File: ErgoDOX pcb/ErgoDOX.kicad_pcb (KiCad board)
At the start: 2 copper layers, 182.8 x 158.9 mm, 77 parts, among them J1 USB, J2 3.5mm, J3 JMP, J4 JMP, SW0:10 SW0:3, SW0:11 SW0:2, SW0:12 SW0:1, SW0:7 SW0:6, SW0:8 SW0:5, SW0:9 SW0:4, SW1:10 SW1:3, SW1:11 SW1:2, SW1:12 SW1:1, SW1:13 SW1:0, SW1:9 SW1:4, SW2:10 SW2:3, SW2:11 SW2:2, SW2:12 SW2:1, SW2:13 SW2:0, SW2:7 SW2:6, SW2:8 SW2:5, SW2:9 SW2:4, SW3:10 SW3:3, SW3:11 SW3:2, SW3:12 SW3:1, SW3:13 SW3:0, SW3:8 SW3:5, SW3:9 SW3:4, SW4:10 SW4:3, SW4:11 SW4:2, SW4:12 SW4:1, SW4:13 SW4:0, SW4:7 SW4:6, SW4:8 SW4:5, SW4:9 SW4:4, SW5:10 SW5:3, SW5:11 SW5:2, SW5:12 SW5:1, SW5:13 SW5:0, SW5:7 SW5:6, SW5:8 SW5:5, SW5:9 SW5:4, U1 TEENSY2.0, U2 MCP23018

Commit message: probably done
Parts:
- removed STAR_1: STAR_FRONT, ErgoDOX pcb:STAR
- removed STAR_2: STAR_BACK, ErgoDOX pcb:STAR
- removed STITCHING_VIA (x11): ~, lib_footprints:STITCHING_VIA
- added H1: D+, Connector_Wire:SolderWirePad_1x01_Drill1mm, F.Cu at (139.1, 40.0)
- added H2: D-, Connector_Wire:SolderWirePad_1x01_Drill1mm, F.Cu at (134.6, 41.3)
- added H3: 5V, Connector_Wire:SolderWirePad_1x01_Drill1mm, F.Cu at (143.5, 39.9)
- added H4: GND, Connector_Wire:SolderWirePad_1x01_Drill1mm, F.Cu at (147.1, 36.1)
- added R3: 5.1kΩ, Resistor_THT:R_Axial_DIN0207_L6.3mm_D2.5mm_P10.16mm_Horizontal, F.Cu at (96.5, 40.6)
- added R4: 5.1kΩ, Resistor_THT:R_Axial_DIN0207_L6.3mm_D2.5mm_P10.16mm_Horizontal, F.Cu at (109.5, 36.6)
- J1: footprint USBMINImod -> Connector_USB:USB_C_Receptacle_GCT_USB4085
- moved J4 48.5 mm to (127.3, 37.1), turned to 180 degrees
- moved J3 33.5 mm to (127.3, 40.9), turned to 180 degrees
- moved R1 33.1 mm to (72.4, 42.2), turned to 45 degrees
- moved R2 28.8 mm to (73.7, 45.5), turned to 45 degrees
- moved J1 6.79 mm to (140.6, 36.6), turned to 180 degrees
- moved RC1 4.64 mm to (130.0, 47.0)
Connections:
- J2 pad 1: Net-(J1-Pad5) -> GND
- J2 pad 4: Net-(J1-Pad1) -> VCC
- J3 pad 1: VCC -> Net-(J1-PadA5)
- J3 pad 2: Net-(J1-Pad5) -> Net-(J3-Pad2)
- J3 pad 3: GND -> Net-(J1-PadA8)
- J4 pad 1: VCC -> Net-(J1-PadB5)
- J4 pad 2: Net-(J1-Pad1) -> Net-(J4-Pad2)
- J4 pad 3: GND -> Net-(J1-PadB8)
- U1 pad 12: Net-(U1-Pad12) -> (no net)
- U1 pad 19: Net-(U1-Pad19) -> (no net)
- U2 pad 14: Net-(U2-Pad14) -> (no net)
- U2 pad 17: Net-(U2-Pad17) -> (no net)
- U2 pad 18: Net-(U2-Pad18) -> (no net)
- U2 pad 19: Net-(U2-Pad19) -> (no net)
- U2 pad 27: Net-(U2-Pad27) -> (no net)
- U2 pad 28: Net-(U2-Pad28) -> (no net)
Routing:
- net Net-(J1-Pad1): track 102.6 -> 0.00 mm
- net Net-(J1-Pad5): track 62.3 -> 0.00 mm
- net GND: track 2.22 -> 32.8 mm, vias 0 -> 49
- net Net-(J3-Pad2): track 0.00 -> 22.9 mm
- net Net-(J4-Pad2): track 0.00 -> 22.2 mm
- net Net-(J1-PadB8): track 0.00 -> 17.2 mm
- net Net-(J1-PadA8): track 0.00 -> 14.1 mm
- net Net-(J1-PadA5): track 0.00 -> 11.2 mm
- net Net-(J1-PadB5): track 0.00 -> 9.89 mm
- net Net-(H2-Pad1): track 0.00 -> 7.49 mm
- net /SCLM: track 119.7 -> 126.8 mm
- net VCC: track 204.8 -> 211.7 mm, vias 2 -> 0
- net /SDAM: track 128.3 -> 135.1 mm
- net Net-(J1-Pad4): track 5.60 -> 0.00 mm
- net Net-(J1-Pad2): track 5.60 -> 0.00 mm
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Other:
- board text removed: "ID"

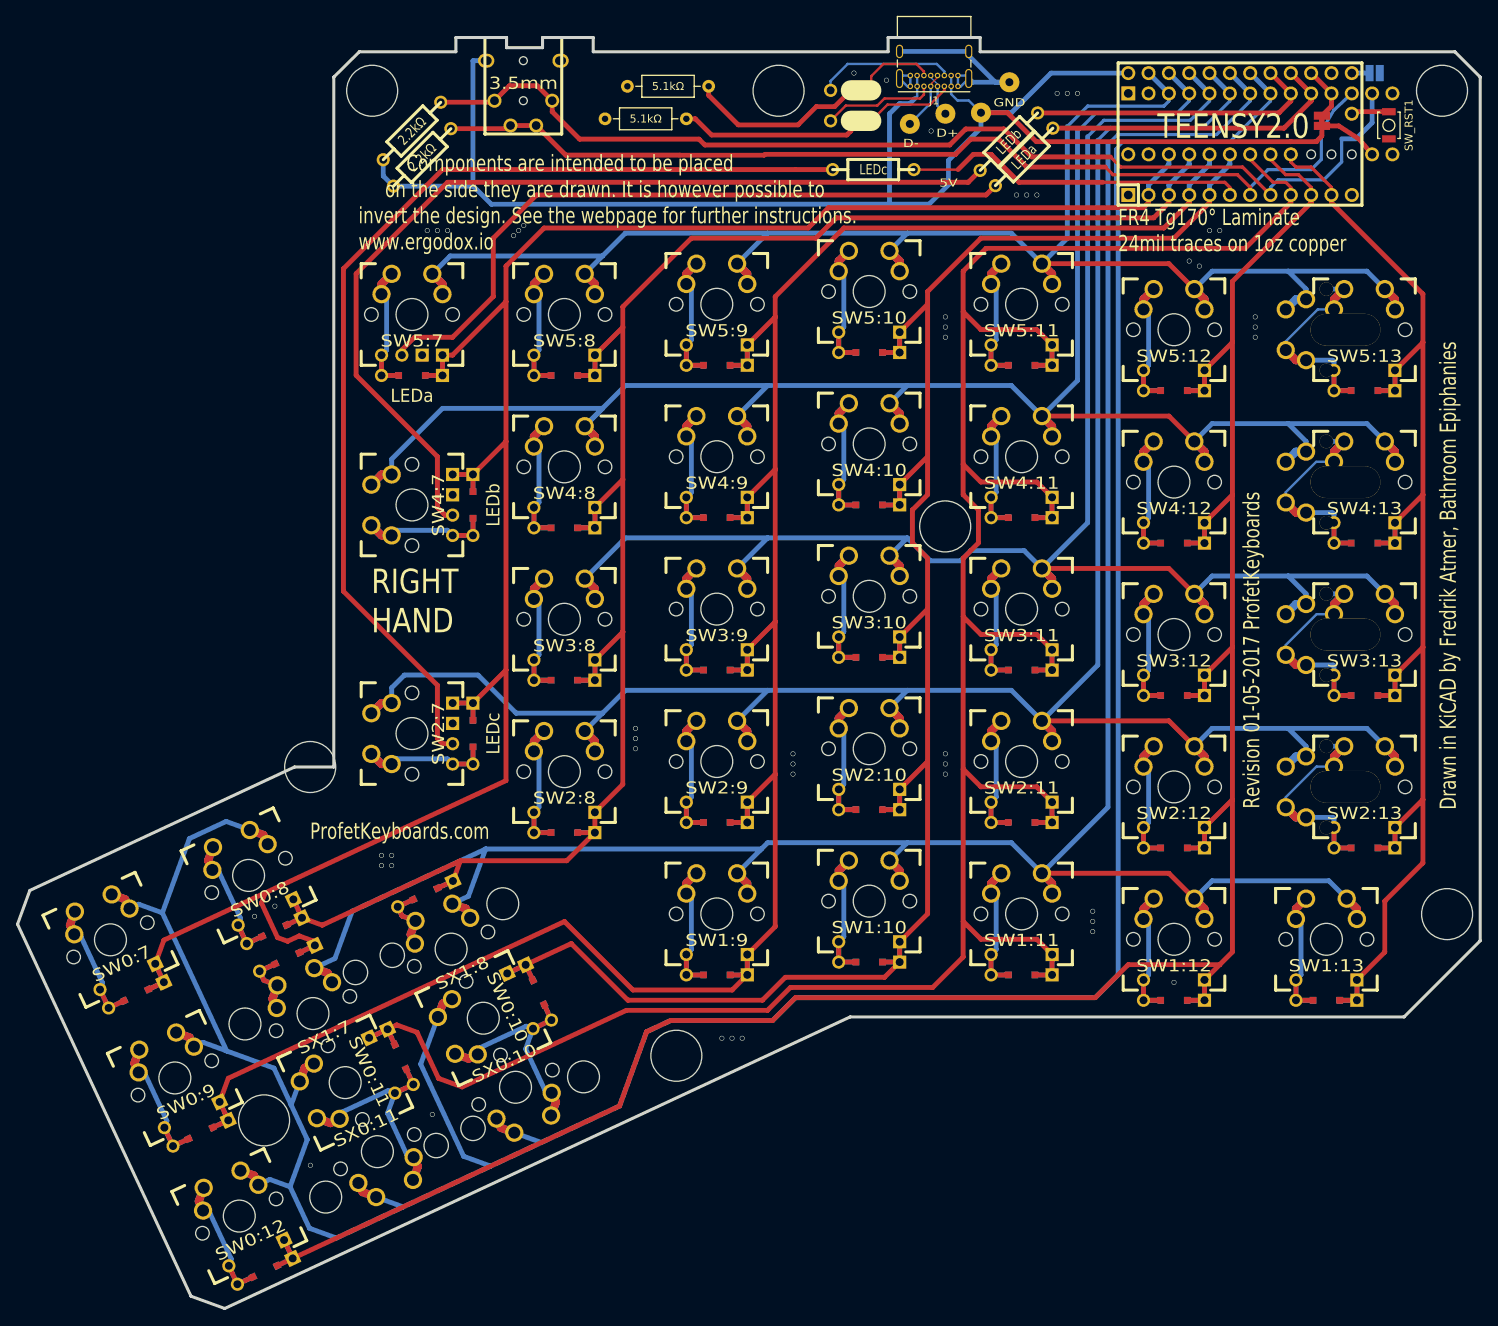
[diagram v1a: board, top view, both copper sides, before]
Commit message: rearranged components to maximize case compatibility
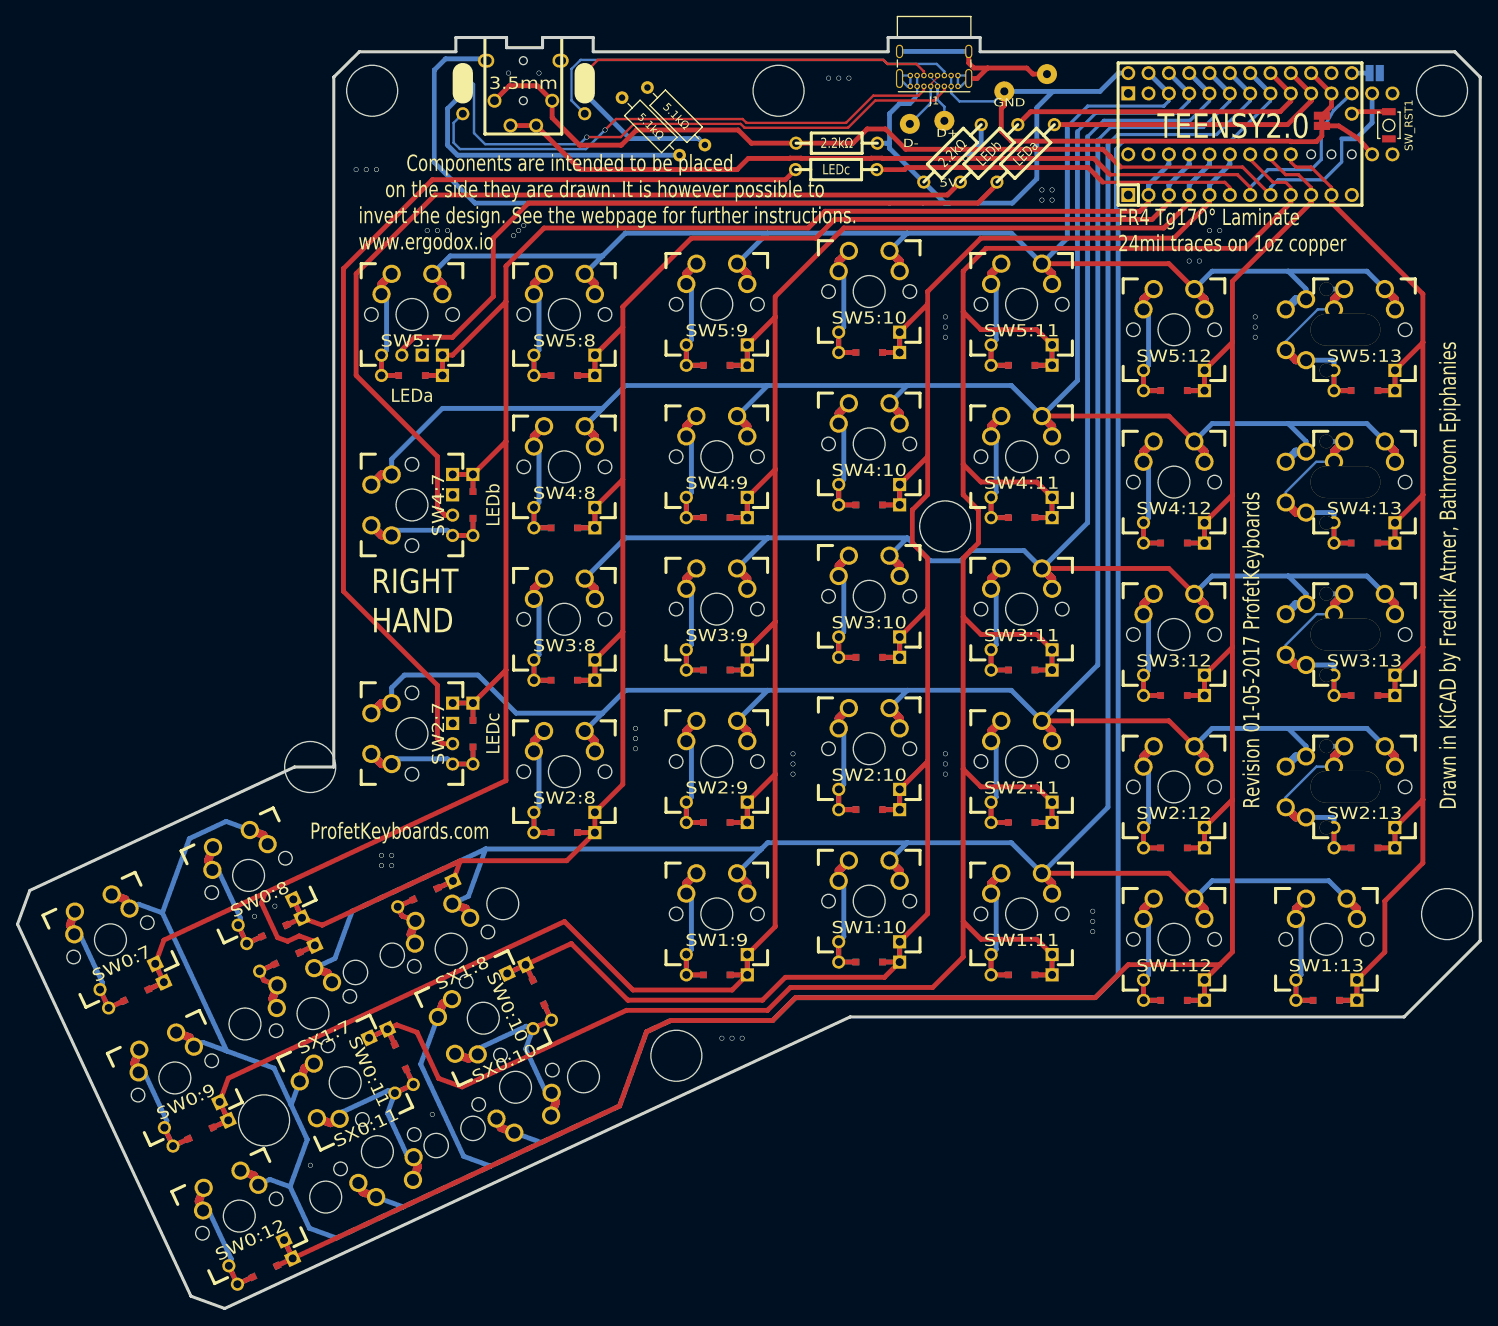
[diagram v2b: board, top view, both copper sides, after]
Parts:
- moved R2 66.3 mm to (140.0, 45.0)
- moved R1 53.1 mm to (125.5, 43.7), turned to 180 degrees
- moved J3 48.6 mm to (78.7, 37.5), turned to 270 degrees
- moved J4 33.3 mm to (94.0, 37.5), turned to 270 degrees
- moved R4 7.35 mm to (109.0, 43.9), turned to 135 degrees
- moved H4 4.81 mm to (151.8, 35.1)
- moved RC1 4.64 mm to (125.4, 47.0)
- moved H3 3.96 mm to (146.4, 37.2)
- moved R3 3.39 mm to (98.6, 38.0), turned to 315 degrees
- moved RB1 2.88 mm to (144.5, 45.0)
- moved H1 0.90 mm to (138.9, 40.9)
- moved RA1 0.48 mm to (149.1, 45.0)
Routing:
- net Net-(J1-PadA5): track 11.2 -> 71.1 mm, vias 0 -> 1
- net Net-(J1-PadA8): track 14.1 -> 67.2 mm, vias 0 -> 1
- net Net-(J1-PadB8): track 17.2 -> 54.4 mm
- net Net-(J1-PadB5): track 9.89 -> 44.2 mm
- net Net-(J3-Pad2): track 22.9 -> 36.8 mm
- net VCC: track 211.7 -> 224.0 mm
- net Net-(LED_C1-Pad1): track 132.1 -> 127.4 mm
- net Net-(J4-Pad2): track 22.2 -> 17.7 mm
- net /LED_C: track 42.9 -> 46.8 mm
- net Net-(LED_B1-Pad1): track 119.1 -> 116.0 mm
- net /LED_B: track 36.8 -> 39.9 mm
- net GND: track 32.8 -> 35.7 mm, vias 49 -> 51
- net /SDAM: track 135.1 -> 132.3 mm
- net /SCLM: track 126.8 -> 124.4 mm, vias 0 -> 1
- net Net-(H1-Pad1): track 5.53 -> 6.37 mm

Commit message: updated silkscreen
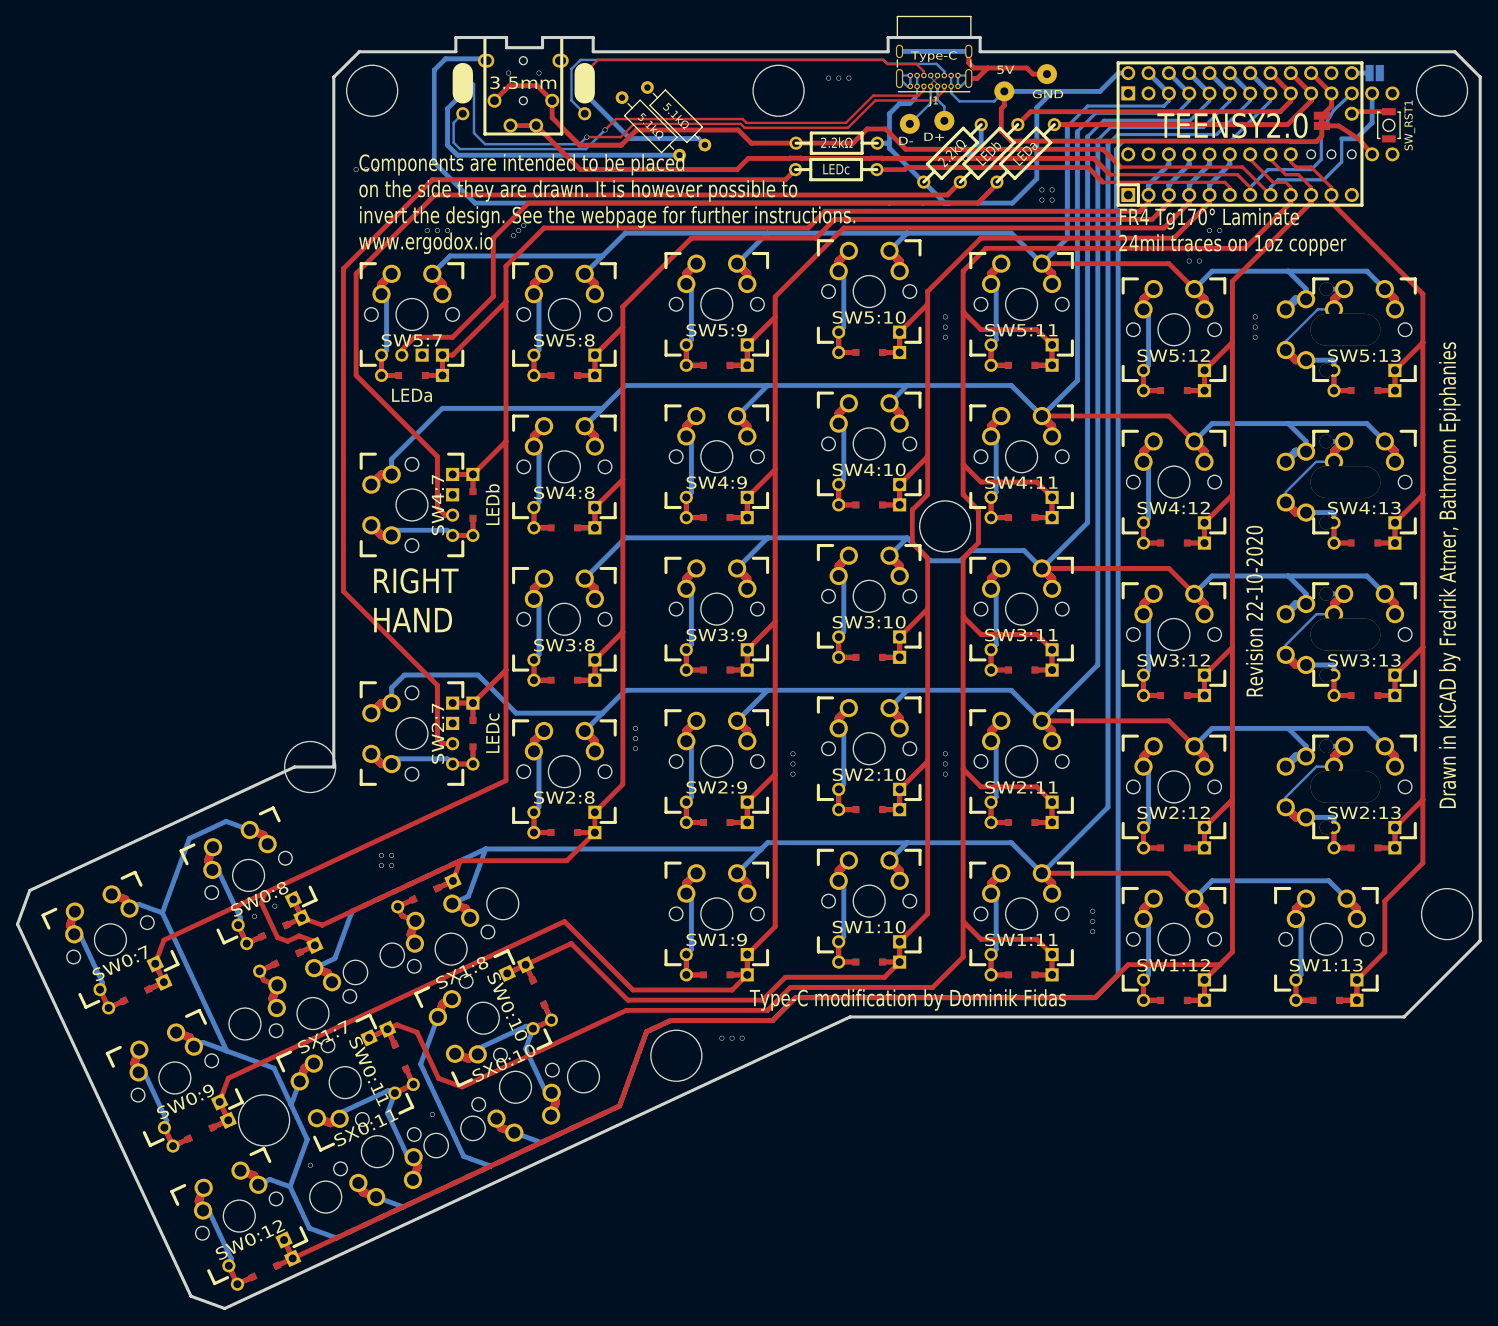
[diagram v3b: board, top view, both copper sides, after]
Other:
- board text added: "Based on Revision 01-05-2017 by ProfetKeyboards"
- board text added: "ErgoDoxOG-C"
- board text added: "Revision 22-10-2020"
- board text added: "Type-C"
- board text added: "Type-C modification by Dominik Fidas"
- board text removed: "ErgoDox"
- board text removed: "ProfetKeyboards.com"
- board text removed: "Revision 01-05-2017 ProfetKeyboards"
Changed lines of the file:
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@@
   (general
     (thickness 1.6002)
-    (drawings 40)
+    (drawings 41)
     (tracks 1341)
     (zones 0)
@@
   (page A4)
   (layers
-    (0 Front signal)
-    (31 Back signal)
+    (0 Front signal hide)
+    (31 Back signal hide)
     (32 B.Adhes user)
     (33 F.Adhes user)
@@
     (35 F.Paste user)
     (36 B.SilkS user hide)
-    (37 F.SilkS user hide)
-    (38 B.Mask user hide)
-    (39 F.Mask user hide)
+    (37 F.SilkS user)
+    (38 B.Mask user)
+    (39 F.Mask user)
     (40 Dwgs.User user)
     (41 Cmts.User user)
@@
       (net 64 /RST))
   )
-  (gr_text 5V (at 139.446 48.641) (layer F.SilkS)
-    (effects (font (size 1.016 1.27) (thickness 0.2032)))
+  (gr_text "Type-C modification by Dominik Fidas" (at 114.6175 150.622) (layer F.SilkS)
+    (effects (font (size 2.032 1.524) (thickness 0.3048)) (justify left))
   )
-  (gr_text GND (at 147.066 38.608) (layer F.SilkS)
-    (effects (font (size 1.016 1.27) (thickness 0.2032)))
+  (gr_text "Revision 22-10-2020" (at 177.8 113.03 90) (layer F.SilkS)
+    (effects (font (size 2.032 1.524) (thickness 0.3048)) (justify left))
   )
-  (gr_text ProfetKeyboards.com (at 70.83 129.73) (layer B.SilkS)
-    (effects (font (size 2.032 1.524) (thickness 0.3048)) (justify mirror))
+  (gr_text Type-C (at 137.668 32.766) (layer F.SilkS)
+    (effects (font (size 1.016 1.2) (thickness 0.2032)))
   )
-  (gr_text ProfetKeyboards.com (at 70.86 129.7) (layer F.SilkS)
-    (effects (font (size 2.032 1.524) (thickness 0.3048)))
+  (gr_text 5V (at 146.558 34.544) (layer F.SilkS)
+    (effects (font (size 1.016 1.27) (thickness 0.2032)))
   )
-  (gr_text "Revision 01-05-2017 ProfetKeyboards" (at 177.36 126.86 90) (layer F.SilkS)
-    (effects (font (size 2.032 1.524) (thickness 0.3048)) (justify left))
+  (gr_text GND (at 151.892 37.592) (layer F.SilkS)
+    (effects (font (size 1.016 1.27) (thickness 0.2032)))
+  )
+  (gr_text "Based on Revision 01-05-2017 by ProfetKeyboards" (at 177.546 68.326 90) (layer B.SilkS)
+    (effects (font (size 2.032 1.524) (thickness 0.3048)) (justify left mirror))
   )
-  (gr_text D+ (at 139.319 42.418) (layer F.SilkS)
+  (gr_text D+ (at 137.668 42.926) (layer F.SilkS)
     (effects (font (size 1.016 1.27) (thickness 0.2032)))
   )
-  (gr_text D- (at 134.747 43.688) (layer F.SilkS)
+  (gr_text D- (at 134.112 43.434) (layer F.SilkS)
     (effects (font (size 1.016 1.27) (thickness 0.2032)))
   )
-  (gr_text ErgoDox (at 113.03 48.895) (layer B.SilkS)
-    (effects (font (size 8.128 12.192) (thickness 2.032)) (justify mirror))
+  (gr_text ErgoDoxOG-C (at 111.506 49.276) (layer B.SilkS)
+    (effects (font (size 8.128 9) (thickness 1.6)) (justify mirror))
   )
-  (gr_text "         Components are intended to be placed\n     on the side they are drawn. It is however possible to\ninvert the design. See the webpage for further instructions.\nwww.ergodox.io" (at 65.7 51.12) (layer F.SilkS)
+  (gr_text "Components are intended to be placed\non the side they are drawn. It is however possible to\ninvert the design. See the webpage for further instructions.\nwww.ergodox.io" (at 65.7 51.12) (layer F.SilkS)
     (effects (font (size 2.032 1.524) (thickness 0.3048)) (justify left))
   )
@@
   (gr_line (start 44.76496 187.81776) (end 48.9839 189.35192) (angle 90) (layer Edge.Cuts) (width 0.381))
   (gr_line (start 48.9839 189.35192) (end 127.1524 152.908) (angle 90) (layer Edge.Cuts) (width 0.381))
-  (via (at 151.13 49.53) (size 0.6096) (drill 0.508) (layers Front Back) (net 19))
-  (via (at 152.4 49.53) (size 0.6096) (drill 0.508) (layers Front Back) (net 19))
-  (via (at 152.4 50.8) (size 0.6096) (drill 0.508) (layers Front Back) (net 19))
-  (via (at 151.13 50.8) (size 0.6096) (drill 0.508) (layers Front Back) (net 19))
   (segment (start 195.2625 72.0852) (end 195.2625 74.6252) (width 0.6096) (layer Back) (net 1))
   (segment (start 195.2625 129.23266) (end 195.2625 131.77266) (width 0.6096) (layer Back) (net 1))
@@
   (segment (start 89.916 40.513) (end 93.345 43.942) (width 0.6096) (layer Front) (net 18))
   (segment (start 89.916 38.3794) (end 89.916 40.513) (width 0.6096) (layer Front) (net 18))
+  (via (at 151.13 49.53) (size 0.6096) (drill 0.508) (layers Front Back) (net 19))
+  (via (at 152.4 49.53) (size 0.6096) (drill 0.508) (layers Front Back) (net 19))
+  (via (at 152.4 50.8) (size 0.6096) (drill 0.508) (layers Front Back) (net 19))
+  (via (at 151.13 50.8) (size 0.6096) (drill 0.508) (layers Front Back) (net 19))
   (segment (start 189.865 34.925) (end 192.0875 34.925) (width 0.6096) (layer Back) (net 19))
   (segment (start 134.6822 35.23) (end 134.6822 36.58) (width 0.3048) (layer Back) (net 19))
